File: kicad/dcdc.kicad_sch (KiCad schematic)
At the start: 48 parts, among them Q1 IPA045N10N3G, Q2 IPA045N10N3G, Q3 IPA045N10N3G, U1 LM5107, U3 MPQ8112

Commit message: major changes
removed Load terminal

changed to 6.3x32mm fuse pcb holder

added LibreSolar kicad footprint library locally
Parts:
- U3: symbol Project:MPQ8112A -> Project:MPQ8112
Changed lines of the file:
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@@
     (pin "1")
   )
-  (symbol (lib_id "Project:MPQ8112A") (at 139.7 134.62 0) (unit 1)
+  (symbol (lib_id "Project:MPQ8112") (at 139.7 134.62 0) (unit 1)
     (in_bom yes) (on_board yes)
     (property "Reference" "U3" (id 0) (at 144.78 127 0))

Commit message: pcb minor fixes, updated bom files, updated project name
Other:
- title: MPPT 2420 HC -> MPPT 4820 HC
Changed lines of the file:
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@@
   (paper "A4")
   (title_block
-    (title "MPPT 2420 HC")
+    (title "MPPT 4820 HC")
     (date "2021-05-03")
     (rev "0.2.3")

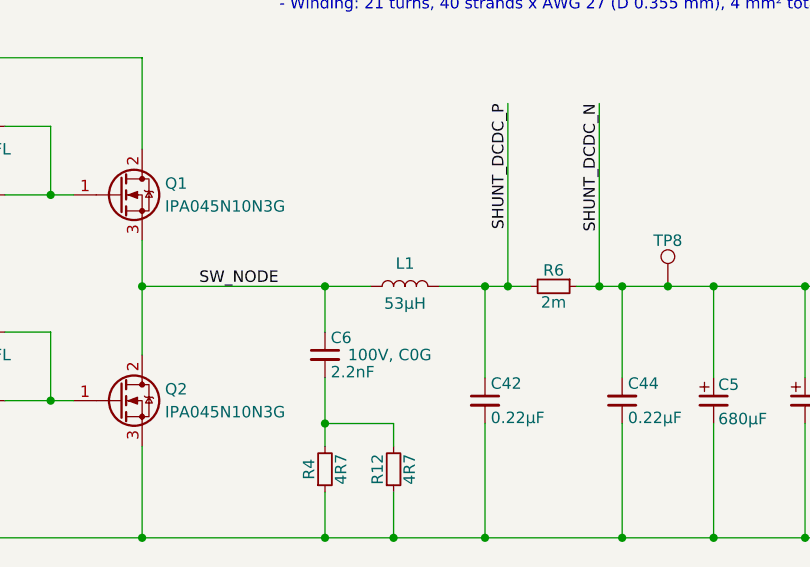
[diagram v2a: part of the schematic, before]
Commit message: updated project to kicad 7
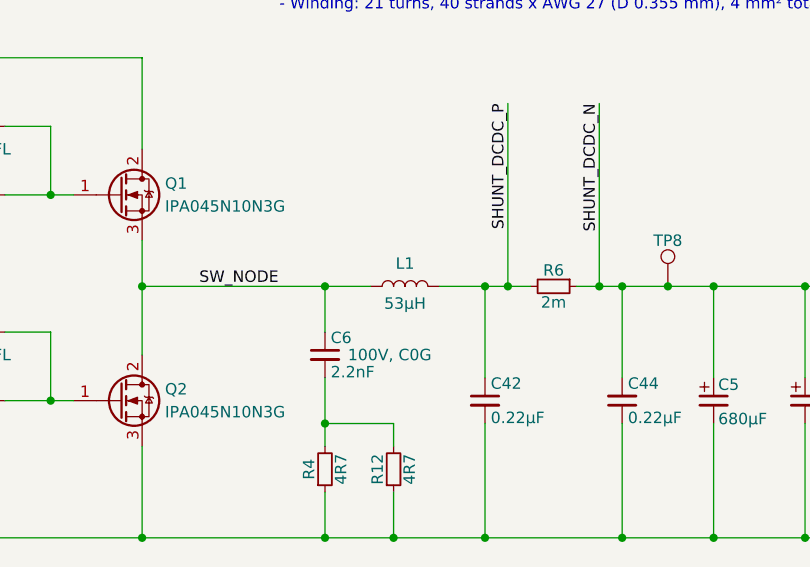
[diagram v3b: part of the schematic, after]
